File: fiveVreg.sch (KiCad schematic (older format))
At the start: 8 parts, among them J1 CONN2, J2 CONN2, J3 CONN3, K1 CONN_3, P1 CONN_1

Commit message: dc converter.
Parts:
- added P2: CONN_1, symbol CONN_1
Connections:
- net GND: now also P2.1
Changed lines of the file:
@@
-EESchema Schematic File Version 2  date Fri 11 Apr 2014 00:16:04 BST
+EESchema Schematic File Version 2
 LIBS:power
 LIBS:device
@@
 LIBS:FE
 LIBS:fiveVreg-cache
-EELAYER 25  0
+EELAYER 27 0
 EELAYER END
-$Descr A4 11700 8267
+$Descr A4 11693 8268
 encoding utf-8
 Sheet 1 1
 Title ""
-Date "10 apr 2014"
+Date "2 may 2014"
 Rev ""
 Comp ""
@@
 F 0 "K1" V 5350 2650 50  0000 C CNN
 F 1 "CONN_3" V 5450 2650 40  0000 C CNN
+F 2 "" H 5400 2650 60  0001 C CNN
+F 3 "" H 5400 2650 60  0001 C CNN
 	1    5400 2650
 	0    -1   -1   0
@@
 F 0 "P1" H 5980 4000 40  0000 L CNN
 F 1 "CONN_1" H 5900 4055 30  0001 C CNN
+F 2 "" H 5900 4000 60  0001 C CNN
+F 3 "" H 5900 4000 60  0001 C CNN
 	1    5900 4000
 	1    0    0    -1
@@
 F 0 "L1" H 4325 2950 30  0000 C CNN
 F 1 "L_MINI" H 4400 3050 22  0000 C CNN
+F 2 "" H 4400 3000 60  0001 C CNN
+F 3 "" H 4400 3000 60  0001 C CNN
 	1    4400 3000
 	1    0    0    -1
@@
 F 0 "C2" H 4725 3725 50  0000 L CNN
 F 1 "C_SMALL" H 4700 3575 50  0000 L CNN
+F 2 "" H 4700 3650 60  0001 C CNN
+F 3 "" H 4700 3650 60  0001 C CNN
 	1    4700 3650
 	1    0    0    -1
@@
 F 0 "C1" H 4025 3725 50  0000 L CNN
 F 1 "C_SMALL" H 4000 3575 50  0000 L CNN
+F 2 "" H 4000 3650 60  0001 C CNN
+F 3 "" H 4000 3650 60  0001 C CNN
 	1    4000 3650
 	1    0    0    -1
@@
 F 0 "#PWR01" H 5950 2840 20  0001 C CNN
 F 1 "+5V" H 5950 2840 30  0000 C CNN
+F 2 "" H 5950 2750 60  0001 C CNN
+F 3 "" H 5950 2750 60  0001 C CNN
 	1    5950 2750
 	1    0    0    -1
@@
 F 0 "#PWR02" H 4000 2750 20  0001 C CNN
 F 1 "+12V" H 4000 2900 30  0000 C CNN
+F 2 "" H 4000 2800 60  0001 C CNN
+F 3 "" H 4000 2800 60  0001 C CNN
 	1    4000 2800
 	1    0    0    -1
@@
 F 0 "#PWR03" H 6650 2440 20  0001 C CNN
 F 1 "+5V" H 6650 2440 30  0000 C CNN
+F 2 "" H 6650 2350 60  0001 C CNN
+F 3 "" H 6650 2350 60  0001 C CNN
 	1    6650 2350
 	1    0    0    -1
@@
 F 0 "#PWR04" H 7200 3350 30  0001 C CNN
 F 1 "GND" H 7200 3280 30  0001 C CNN
+F 2 "" H 7200 3350 60  0001 C CNN
+F 3 "" H 7200 3350 60  0001 C CNN
 	1    7200 3350
 	1    0    0    -1
@@
 F 0 "#PWR05" H 5400 4200 30  0001 C CNN
 F 1 "GND" H 5400 4130 30  0001 C CNN
+F 2 "" H 5400 4200 60  0001 C CNN
+F 3 "" H 5400 4200 60  0001 C CNN
 	1    5400 4200
 	1    0    0    -1
@@
 F 0 "#PWR06" H 3400 2200 20  0001 C CNN
 F 1 "+12V" H 3400 2350 30  0000 C CNN
+F 2 "" H 3400 2250 60  0001 C CNN
+F 3 "" H 3400 2250 60  0001 C CNN
 	1    3400 2250
 	1    0    0    -1
@@
 F 0 "#PWR07" H 2800 3350 20  0001 C CNN
 F 1 "+12V" H 2800 3500 30  0000 C CNN
+F 2 "" H 2800 3400 60  0001 C CNN
+F 3 "" H 2800 3400 60  0001 C CNN
 	1    2800 3400
 	1    0    0    -1
@@
 F 0 "#PWR08" H 3400 2950 30  0001 C CNN
 F 1 "GND" H 3400 2880 30  0001 C CNN
+F 2 "" H 3400 2950 60  0001 C CNN
+F 3 "" H 3400 2950 60  0001 C CNN
 	1    3400 2950
 	1    0    0    -1
@@
 F 0 "#PWR09" H 2800 4050 30  0001 C CNN
 F 1 "GND" H 2800 3980 30  0001 C CNN
+F 2 "" H 2800 4050 60  0001 C CNN
+F 3 "" H 2800 4050 60  0001 C CNN
 	1    2800 4050
 	1    0    0    -1
@@
 F 0 "J3" H 6750 3050 50  0000 C CNN
 F 1 "CONN3" V 6800 3250 40  0000 C CNN
+F 2 "" H 6750 3250 60  0001 C CNN
+F 3 "" H 6750 3250 60  0001 C CNN
 	1    6750 3250
 	0    1    1    0
@@
 F 0 "J2" H 3400 3650 40  0000 C CNN
 F 1 "CONN2" V 3550 3800 40  0000 C CNN
+F 2 "" H 3400 3750 60  0001 C CNN
+F 3 "" H 3400 3750 60  0001 C CNN
 	1    3400 3750
 	1    0    0    -1
@@
 F 0 "J1" H 2950 2450 40  0000 C CNN
 F 1 "CONN2" V 3100 2600 40  0000 C CNN
+F 2 "" H 2950 2550 60  0001 C CNN
+F 3 "" H 2950 2550 60  0001 C CNN
 	1    2950 2550
 	-1   0    0    1
 $EndComp
+$Comp
+L CONN_1 P2
+U 1 1 53639E34
+P 5900 3900
+F 0 "P2" H 5980 3900 40  0000 L CNN
+F 1 "CONN_1" H 5900 3955 30  0001 C CNN
+F 2 "" H 5900 3900 60  0001 C CNN
+F 3 "" H 5900 3900 60  0001 C CNN
+	1    5900 3900
+	1    0    0    -1
+$EndComp
+Wire Wire Line
+	5750 3900 5400 3900
+Connection ~ 5400 3900
 $EndSCHEMATC

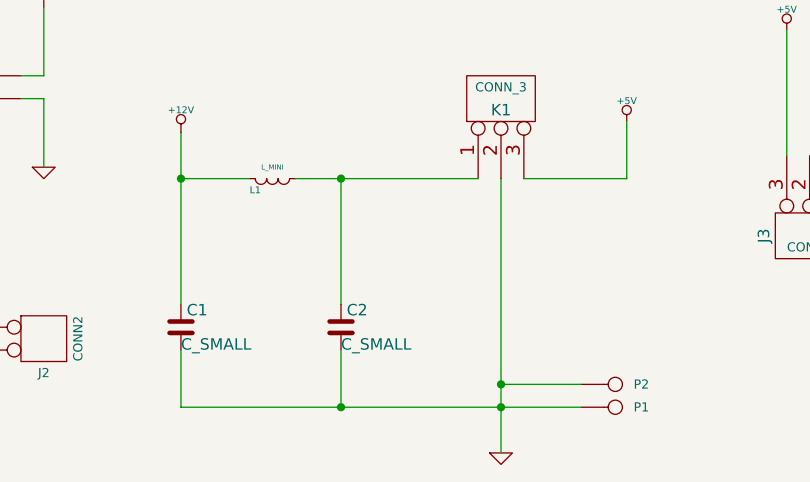
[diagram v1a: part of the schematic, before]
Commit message: Fit for Duet 0.6
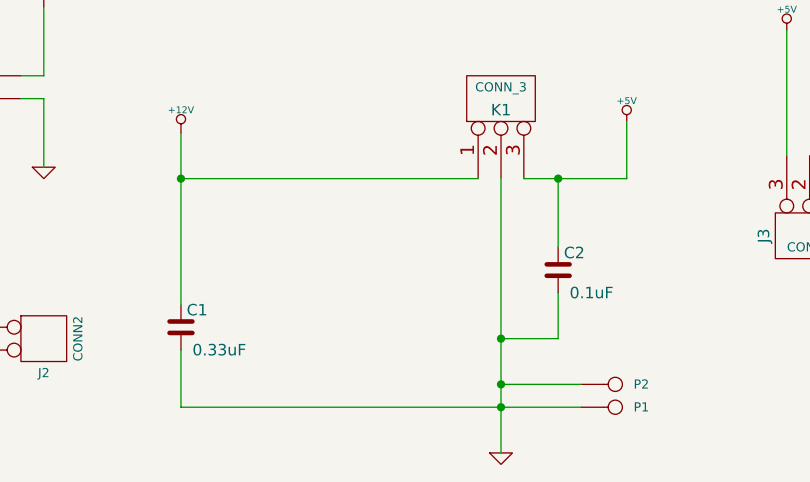
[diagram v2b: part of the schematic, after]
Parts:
- removed L1: L_MINI, symbol L_MINI
- C1: value C_SMALL -> 0.33uF
- C2: value C_SMALL -> 0.1uF
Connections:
- net +12V: now also K1.1 (P1)
- net +5V: now also C2.1
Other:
- moved on the sheet: C2
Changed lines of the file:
@@
 Sheet 1 1
 Title ""
-Date "2 may 2014"
+Date "11 may 2014"
 Rev ""
 Comp ""
@@
 	5500 3000 5950 3000
 Wire Wire Line
-	5300 3000 4500 3000
+	4000 3000 5300 3000
 Wire Wire Line
 	2800 4050 2800 3750
@@
 Connection ~ 5400 4000
 Wire Wire Line
-	4700 4000 4700 3750
-Connection ~ 4700 3000
-Wire Wire Line
-	4700 3550 4700 3000
-Wire Wire Line
-	4000 3000 4300 3000
-Wire Wire Line
 	3400 2950 3400 2650
 Wire Wire Line
@@
 Wire Wire Line
 	4000 3750 4000 4000
-Connection ~ 4700 4000
 Wire Wire Line
 	3050 3650 2800 3650
@@
 $EndComp
 $Comp
-L L_MINI L1
-U 1 1 53471582
-P 4400 3000
-F 0 "L1" H 4325 2950 30  0000 C CNN
-F 1 "L_MINI" H 4400 3050 22  0000 C CNN
-F 2 "" H 4400 3000 60  0001 C CNN
-F 3 "" H 4400 3000 60  0001 C CNN
-	1    4400 3000
-	1    0    0    -1
-$EndComp
-$Comp
 L C_SMALL C2
 U 1 1 53471531
-P 4700 3650
-F 0 "C2" H 4725 3725 50  0000 L CNN
-F 1 "C_SMALL" H 4700 3575 50  0000 L CNN
-F 2 "" H 4700 3650 60  0001 C CNN
-F 3 "" H 4700 3650 60  0001 C CNN
-	1    4700 3650
+P 5650 3400
+F 0 "C2" H 5675 3475 50  0000 L CNN
+F 1 "0.1uF" H 5700 3300 50  0000 L CNN
+F 2 "" H 5650 3400 60  0001 C CNN
+F 3 "" H 5650 3400 60  0001 C CNN
+	1    5650 3400
 	1    0    0    -1
 $EndComp
@@
 P 4000 3650
 F 0 "C1" H 4025 3725 50  0000 L CNN
-F 1 "C_SMALL" H 4000 3575 50  0000 L CNN
+F 1 "0.33uF" H 4050 3550 50  0000 L CNN
 F 2 "" H 4000 3650 60  0001 C CNN
 F 3 "" H 4000 3650 60  0001 C CNN
@@
 	5750 3900 5400 3900
 Connection ~ 5400 3900
+Wire Wire Line
+	5650 3300 5650 3000
+Connection ~ 5650 3000
+Wire Wire Line
+	5650 3500 5650 3700
+Wire Wire Line
+	5650 3700 5400 3700
+Connection ~ 5400 3700
 $EndSCHEMATC

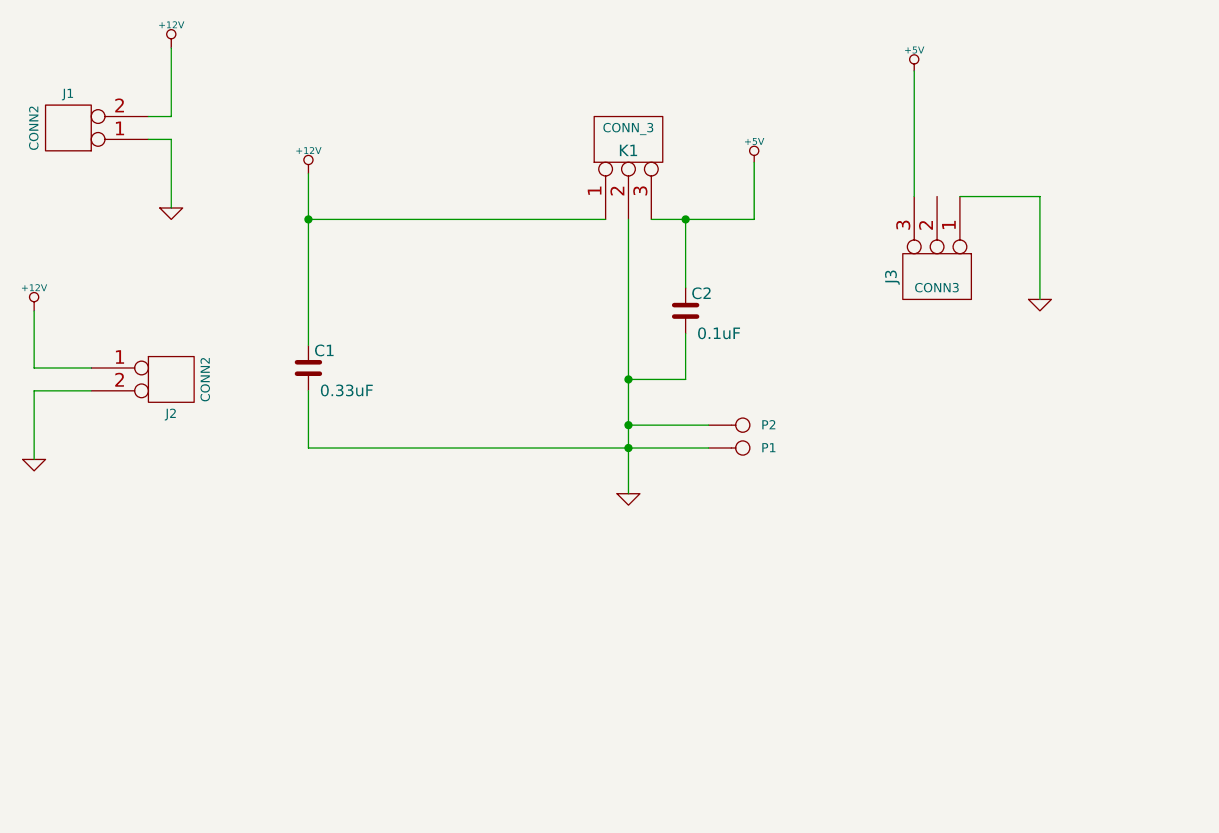
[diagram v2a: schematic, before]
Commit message: Modified for dual motor Z axes and 12v pass through.
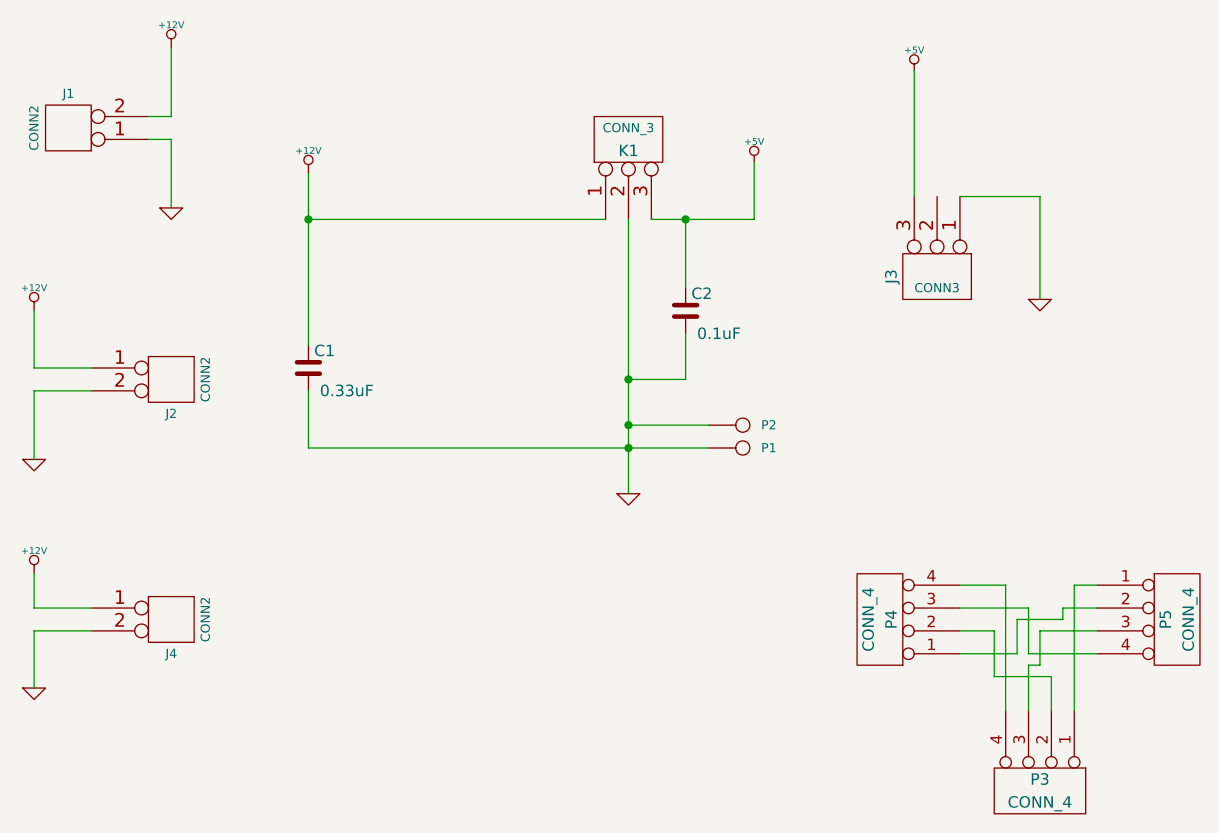
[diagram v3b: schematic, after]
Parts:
- added J4: CONN2, symbol CONN2
- added P3, P4, P5: CONN_4, symbol CONN_4
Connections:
- net +12V: now also J4.1 (P1)
- net GND: now also J4.2 (PM)
- new net: P3.1 (P1), P5.1 (P1)
- new net: P4.1 (P1), P5.2 (P2)
- new net: P3.3 (P3), P5.3 (P3)
- new net: P4.3 (P3), P5.4 (P4)
- new net: P3.2 (P2), P4.2 (P2)
- new net: P3.4 (P4), P4.4 (P4)
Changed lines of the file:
@@
 Sheet 1 1
 Title ""
-Date "11 may 2014"
+Date "15 oct 2014"
 Rev ""
 Comp ""
@@
 	5650 3700 5400 3700
 Connection ~ 5400 3700
+$Comp
+L CONN2 J4
+U 1 1 543D2FDB
+P 3400 4800
+F 0 "J4" H 3400 4700 40  0000 C CNN
+F 1 "CONN2" V 3550 4850 40  0000 C CNN
+F 2 "" H 3400 4800 60  0001 C CNN
+F 3 "" H 3400 4800 60  0001 C CNN
+	1    3400 4800
+	1    0    0    -1
+$EndComp
+$Comp
+L GND #PWR010
+U 1 1 543D2FE1
+P 2800 5050
+F 0 "#PWR010" H 2800 5050 30  0001 C CNN
+F 1 "GND" H 2800 4980 30  0001 C CNN
+F 2 "" H 2800 5050 60  0001 C CNN
+F 3 "" H 2800 5050 60  0001 C CNN
+	1    2800 5050
+	1    0    0    -1
+$EndComp
+$Comp
+L +12V #PWR011
+U 1 1 543D2FE7
+P 2800 4550
+F 0 "#PWR011" H 2800 4500 20  0001 C CNN
+F 1 "+12V" H 2800 4650 30  0000 C CNN
+F 2 "" H 2800 4550 60  0001 C CNN
+F 3 "" H 2800 4550 60  0001 C CNN
+	1    2800 4550
+	1    0    0    -1
+$EndComp
+Wire Wire Line
+	3050 4800 2800 4800
+Wire Wire Line
+	2800 4800 2800 5050
+Wire Wire Line
+	3050 4700 2800 4700
+Wire Wire Line
+	2800 4700 2800 4550
+$Comp
+L CONN_4 P5
+U 1 1 543E3904
+P 7800 4750
+F 0 "P5" V 7750 4750 50  0000 C CNN
+F 1 "CONN_4" V 7850 4750 50  0000 C CNN
+F 2 "" H 7800 4750 60  0000 C CNN
+F 3 "" H 7800 4750 60  0000 C CNN
+	1    7800 4750
+	1    0    0    -1
+$EndComp
+$Comp
+L CONN_4 P4
+U 1 1 543E3913
+P 6500 4750
+F 0 "P4" V 6450 4750 50  0000 C CNN
+F 1 "CONN_4" V 6550 4750 50  0000 C CNN
+F 2 "" H 6500 4750 60  0000 C CNN
+F 3 "" H 6500 4750 60  0000 C CNN
+	1    6500 4750
+	-1   0    0    1
+$EndComp
+$Comp
+L CONN_4 P3
+U 1 1 543E3922
+P 7200 5500
+F 0 "P3" V 7150 5500 50  0000 C CNN
+F 1 "CONN_4" V 7250 5500 50  0000 C CNN
+F 2 "" H 7200 5500 60  0000 C CNN
+F 3 "" H 7200 5500 60  0000 C CNN
+	1    7200 5500
+	0    1    1    0
+$EndComp
+Wire Wire Line
+	6850 4600 7050 4600
+Wire Wire Line
+	7050 4600 7050 5150
+Wire Wire Line
+	6850 4700 7150 4700
+Wire Wire Line
+	7150 4700 7150 4900
+Wire Wire Line
+	7150 4900 7450 4900
+Wire Wire Line
+	6850 4800 7000 4800
+Wire Wire Line
+	7000 4800 7000 5000
+Wire Wire Line
+	7000 5000 7250 5000
+Wire Wire Line
+	7250 5000 7250 5150
+Wire Wire Line
+	6850 4900 7100 4900
+Wire Wire Line
+	7100 4900 7100 4750
+Wire Wire Line
+	7100 4750 7300 4750
+Wire Wire Line
+	7300 4750 7300 4700
+Wire Wire Line
+	7300 4700 7450 4700
+Wire Wire Line
+	7450 4600 7350 4600
+Wire Wire Line
+	7350 4600 7350 5150
+Wire Wire Line
+	7450 4800 7200 4800
+Wire Wire Line
+	7200 4800 7200 4950
+Wire Wire Line
+	7200 4950 7150 4950
+Wire Wire Line
+	7150 4950 7150 5150
 $EndSCHEMATC
